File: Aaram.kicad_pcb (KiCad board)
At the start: 2 copper layers, 100 x 100 mm, 52 parts, among them J1 Conn_01x03, J2 Conn_01x02, J3 AC_OUT, J4 SWITCH_IN, J5 5V_OUT, J6 PSU_AC_IN, J8 SPARE_PINS, K1 10A cube relay, K2 10A cube relay, K3 10A cube relay, Q1 BT136-600, Q2 2N2222A, Q3 2N2222A, Q4 2N2222A, U1 ESP32-DevKitC, U2 TLP281-4GB_F_

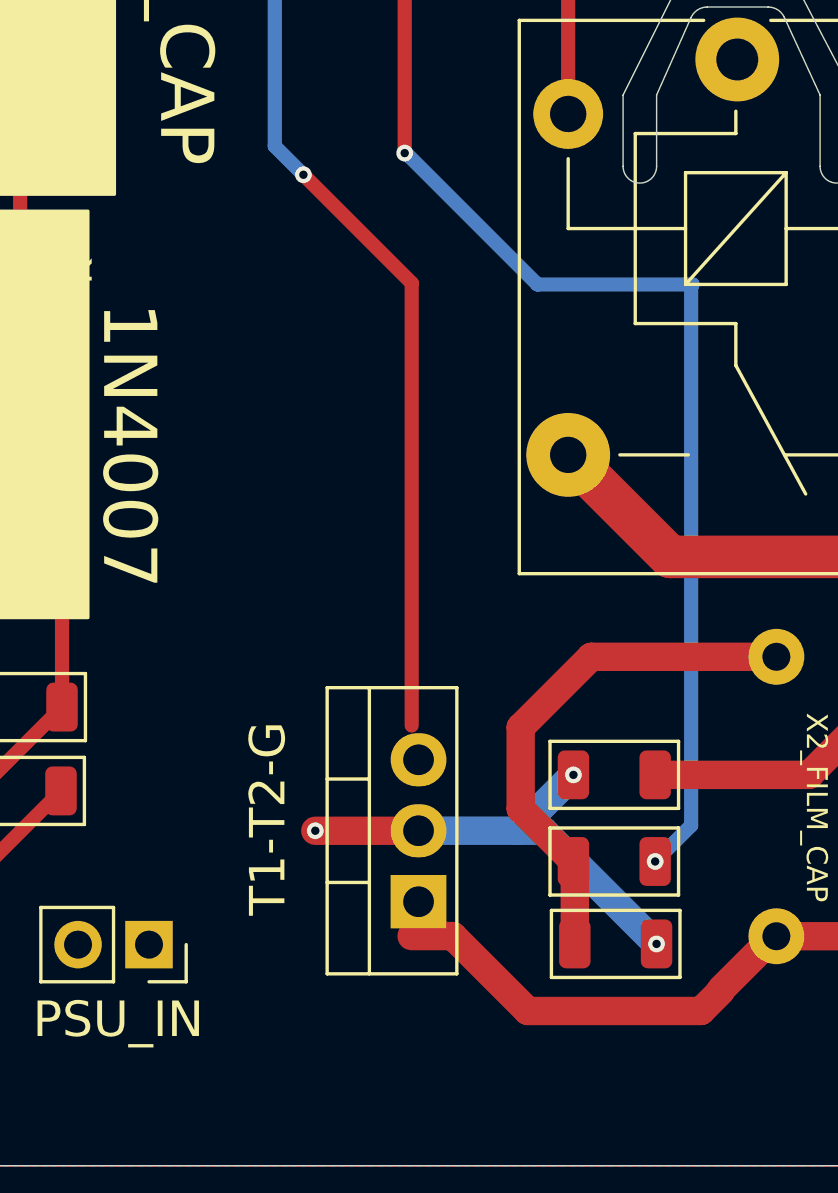
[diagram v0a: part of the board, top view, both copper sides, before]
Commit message: Fixed unconnected tracks of triac
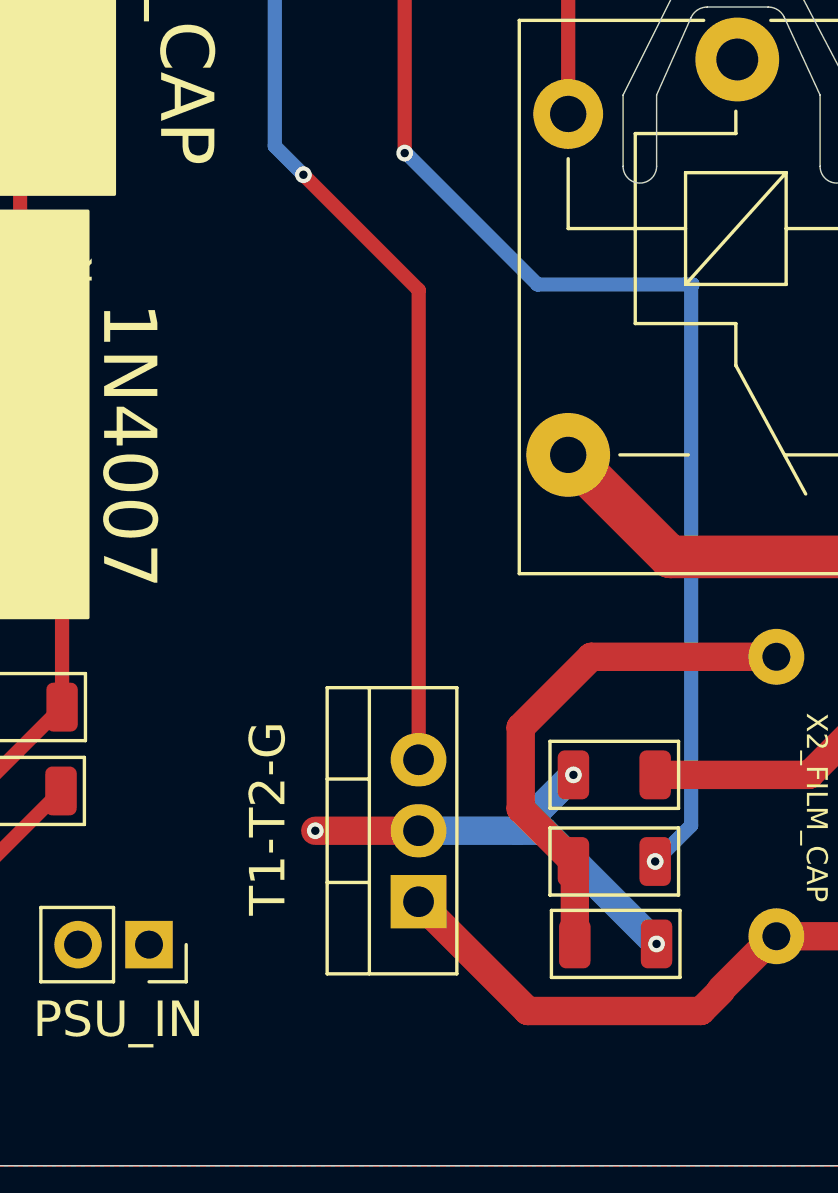
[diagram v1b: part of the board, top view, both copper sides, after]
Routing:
- net Net-(Q1-G): track 58.8 -> 60.1 mm
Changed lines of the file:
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@@
+	)
+	(segment
+		(start 118.313 126.637)
+		(end 117.6 127.35)
+		(width 1.016)
+		(layer "F.Cu")
+		(net 1)
 	)
 	(segment
@@
 	)
 	(segment
-		(start 118.313 126.637)
-		(end 117.6 127.35)
-		(width 1.016)
-		(layer "F.Cu")
-		(net 1)
-	)
-	(segment
-		(start 108.725 124.67)
-		(end 107.245 124.67)
-		(width 1.016)
-		(layer "F.Cu")
-		(net 1)
-	)
-	(segment
-		(start 111.405 127.35)
-		(end 108.725 124.67)
-		(width 1.016)
-		(layer "F.Cu")
-		(net 1)
-	)
-	(segment
 		(start 118.313 126.587)
 		(end 118.313 126.637)
@@
 		(start 117.6 127.35)
 		(end 111.405 127.35)
+		(width 1.016)
+		(layer "F.Cu")
+		(net 1)
+	)
+	(segment
+		(start 111.405 127.35)
+		(end 107.495 123.44)
 		(width 1.016)
 		(layer "F.Cu")
@@
 	)
 	(segment
-		(start 107.25 101.3)
-		(end 107.25 117.135)
+		(start 107.5 101.55)
+		(end 107.5 118.355)
 		(width 0.508)
 		(layer "F.Cu")
@@
 	(segment
 		(start 103.375 97.425)
-		(end 107.25 101.3)
-		(width 0.508)
-		(layer "F.Cu")
+		(end 107.5 101.55)
+		(width 0.508)
+		(layer "F.Cu")
+		(net 40)
+	)
+	(segment
+		(start 107.5 118.355)
+		(end 107.495 118.36)
+		(width 0.508)
+		(layer "F.Cu")

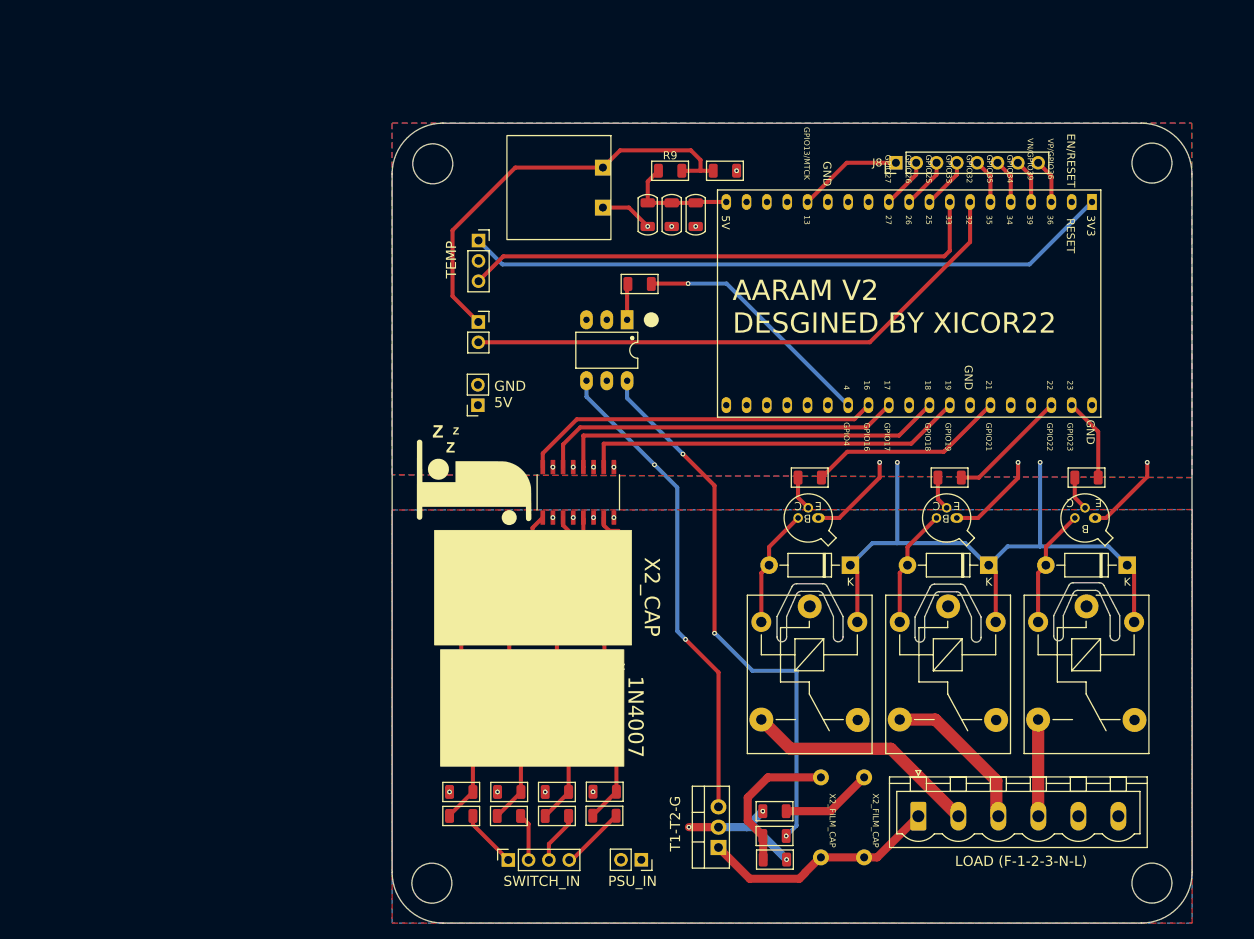
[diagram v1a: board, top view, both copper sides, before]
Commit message: Updated Silkscreen and connections
Moved the fan control from GPIO4 to GPIO 13, made changes to the silkscreen and redid some of the tracks for better layout.
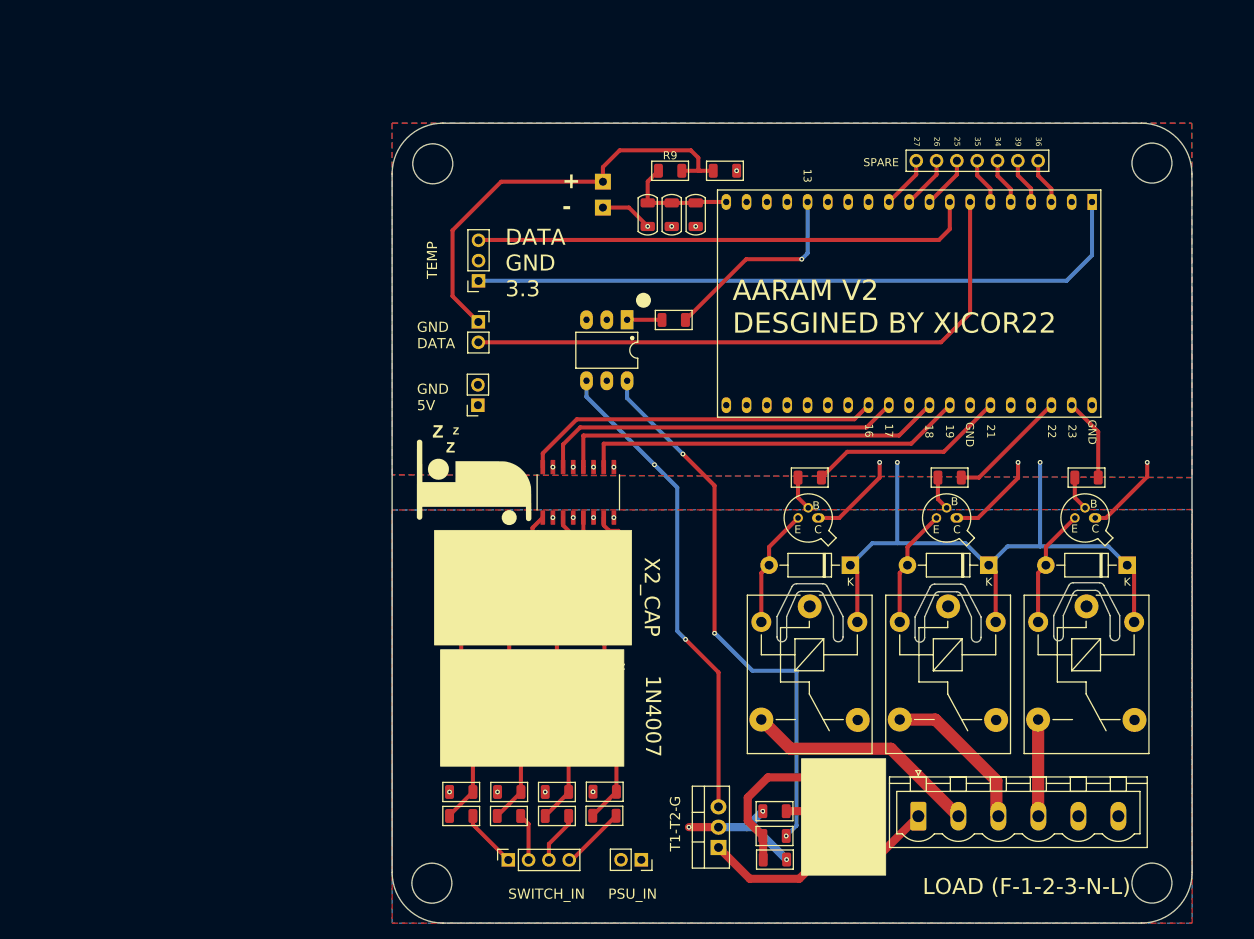
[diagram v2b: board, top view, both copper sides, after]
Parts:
- moved R4 6.20 mm to (101.9, 57.5)
- moved J1 5.05 mm to (77.5, 52.6), turned to 180 degrees
- moved J8 0.25 mm to (129.7, 37.6)
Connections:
- U1 pad 15: SP1 -> T1_Pin
- U1 pad 26: T1_Pin -> unconnected-(U1-ADC2_CH0/GPIO4-Pad26)
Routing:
- net SP1: track 13.1 -> 0.00 mm
- net T1_Pin: track 30.9 -> 25.1 mm
- net S2_Pin: track 71.7 -> 76.9 mm
- net S1_Pin: track 66.6 -> 62.8 mm
- net +3.3V: track 81.2 -> 84.6 mm
- net Net-(J2-Pin_1): track 53.7 -> 54.7 mm
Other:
- board text added: "+ -"
- board text added: "DATA GND 3.3"
- board text added: "GND DATA"
- board text added: "SPARE"

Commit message: Component update
Changed most of the components to use SMD form factor, updated clearance between components in the AC zone and updated the tracks.
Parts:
- C10, C8, C9: footprint PCM_Capacitor_SMD_AKL:C_1206_3216Metric -> PCM_Capacitor_SMD_Handsoldering_AKL:C_1206_3216Metric_Pad1.42x1.75mm
- D1, D2, D3, D4, D5, D6, D7: footprint Diode_THT:D_DO-41_SOD81_P10.16mm_Horizontal -> Diode_SMD:D_SMA_Handsoldering
- Q2, Q3, Q4: footprint PCM_Package_TO_SOT_THT_AKL:TO-18-3_EBC -> PCM_Package_TO_SOT_SMD_AKL:SOT-23_BigPads
- R1, R10, R11, R12, R13, R14, R15, R16, R17, R2, R3, R4, R5, R6, R7, R8, R9: footprint PCM_Resistor_SMD_AKL:R_1206_3216Metric -> PCM_Capacitor_SMD_Handsoldering_AKL:C_1206_3216Metric_Pad1.42x1.75mm
- moved R7 6.07 mm to (112.0, 119.4), turned to 0 degrees
- moved Q1 5.78 mm to (105.2, 118.2)
- moved D3 4.85 mm to (119.5, 86.4)
- moved D1 4.77 mm to (154.1, 86.5)
- moved D2 4.75 mm to (136.8, 86.5)
- moved R5 4.07 mm to (112.1, 115.6)
- moved D4 3.89 mm to (75.4, 104.8)
- moved D5 3.89 mm to (81.4, 104.8)
- moved D6 3.89 mm to (93.3, 104.8)
- moved D7 3.89 mm to (87.4, 104.8)
- moved R6 2.83 mm to (112.1, 123.5), turned to 180 degrees
- moved R11 2.64 mm to (75.3, 113.9)
- moved R13 2.64 mm to (81.3, 113.9)
- moved R15 2.64 mm to (93.3, 113.8)
- moved R17 2.64 mm to (87.3, 113.9)
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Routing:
- net LOAD_F: track 29.9 -> 37.5 mm
- net AC_L: track 16.7 -> 9.27 mm, vias 3 -> 2
- net Net-(C1-Pad1): track 18.7 -> 11.9 mm
- net Net-(Q1-G): track 60.1 -> 53.8 mm, vias 2 -> 1
- net Net-(C4-Pad1): track 11.5 -> 17.2 mm, vias 0 -> 1
- net +5V: track 96.2 -> 101.3 mm, vias 2 -> 5
- net Net-(D6-A): track 10.2 -> 14.0 mm
- net Net-(D4-A): track 10.2 -> 14.0 mm
- net Net-(D5-A): track 10.2 -> 14.0 mm
- net Net-(D7-A): track 10.2 -> 13.9 mm
- net Net-(OC1-Pad6): track 69.5 -> 72.4 mm, vias 3 -> 4
- net GND: track 41.0 -> 39.0 mm
- net Net-(D4-K): track 22.9 -> 24.7 mm
- net Net-(D5-K): track 22.8 -> 24.4 mm
- net D3: track 10.4 -> 8.97 mm
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
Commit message: Updated mostly everything
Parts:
- removed C10, C8, C9: 22uf, PCM_Capacitor_SMD_Handsoldering_AKL:C_1206_3216Metric_Pad1.42x1.75mm
- removed C3, C5: CP_Axial_L10.0mm_D4.5mm_P15.00mm, Xicor_Custom stuff:Axial_Capacitor_P10mm_W4.5mm
- removed D4, D5, D6, D7: 1N4007, Diode_SMD:D_SMA_Handsoldering
- removed G***: LOGO, LOGO
- removed R11, R13: 10K, PCM_Capacitor_SMD_Handsoldering_AKL:C_1206_3216Metric_Pad1.42x1.75mm
- removed R16: 1M, PCM_Capacitor_SMD_Handsoldering_AKL:C_1206_3216Metric_Pad1.42x1.75mm
- added C11: 10uf, PCM_Capacitor_SMD_Handsoldering_AKL:C_1206_3216Metric_Pad1.42x1.75mm, F.Cu at (65.6, 57.4)
- added C12: 10uf, PCM_Capacitor_SMD_Handsoldering_AKL:C_1206_3216Metric_Pad1.42x1.75mm, F.Cu at (65.6, 60.6)
- added C16: 1uf, PCM_Capacitor_SMD_Handsoldering_AKL:C_1206_3216Metric_Pad1.42x1.75mm, F.Cu at (113.7, 47.9)
- added C18: 0.1uf, PCM_Capacitor_SMD_Handsoldering_AKL:C_1206_3216Metric_Pad1.42x1.75mm, F.Cu at (87.7, 40.8)
- added C19: 0.1uf, PCM_Capacitor_SMD_Handsoldering_AKL:C_1206_3216Metric_Pad1.42x1.75mm, F.Cu at (96.2, 49.6)
- added D10: MB6S, PCM_Diode_SMD_AKL:Diode_Bridge_MBS, F.Cu at (108.4, 92.4)
- added D11: MB6S, PCM_Diode_SMD_AKL:Diode_Bridge_MBS, F.Cu at (115.1, 92.4)
- added D8: MB6S, PCM_Diode_SMD_AKL:Diode_Bridge_MBS, F.Cu at (94.8, 92.4)
- added D9: MB6S, PCM_Diode_SMD_AKL:Diode_Bridge_MBS, F.Cu at (101.6, 92.4)
- added F1: Fuse, Xicor_Custom stuff:BLX-A, F.Cu at (43.5, 113.3)
- added J10: Conn_01x03_Socket, Connector_JST:JST_SH_BM03B-SRSS-TB_1x03-1MP_P1.00mm_Vertical, F.Cu at (115.8, 61.1)
- added J11: Conn_01x03_Socket, Connector_JST:JST_SH_BM03B-SRSS-TB_1x03-1MP_P1.00mm_Vertical, F.Cu at (105.1, 61.1)
- added J12: Conn_01x03_Socket, Connector_JST:JST_SH_BM03B-SRSS-TB_1x03-1MP_P1.00mm_Vertical, F.Cu at (105.1, 53.5)
- added J13: Conn_01x03_Socket, Connector_JST:JST_SH_BM03B-SRSS-TB_1x03-1MP_P1.00mm_Vertical, F.Cu at (115.8, 53.5)
- added J7: Conn_01x05, Connector_PinHeader_2.54mm:PinHeader_1x05_P2.54mm_Vertical, F.Cu at (72.6, 22.7)
- added J9: Conn_01x02, Connector_PinSocket_2.54mm:PinSocket_1x02_P2.54mm_Vertical, F.Cu at (22.8, 33.8)
- added R19: 100K, PCM_Resistor_SMD_AKL:R_1206_3216Metric_Pad1.42x1.75mm_HandSolder, F.Cu at (115.7, 82.4)
- added R20: 10K, PCM_Resistor_SMD_AKL:R_1206_3216Metric_Pad1.42x1.75mm_HandSolder, B.Cu at (115.8, 53.6)
- added R21: 10k, PCM_Resistor_SMD_AKL:R_1206_3216Metric_Pad1.42x1.75mm_HandSolder, F.Cu at (96.2, 46.6)
- added R22: 10k, PCM_Resistor_SMD_AKL:R_1206_3216Metric_Pad1.42x1.75mm_HandSolder, F.Cu at (102.9, 40.3)
- added R23: 100K, PCM_Resistor_SMD_AKL:R_1206_3216Metric_Pad1.42x1.75mm_HandSolder, F.Cu at (107.1, 82.4)
- added R25: 10K, PCM_Resistor_SMD_AKL:R_1206_3216Metric_Pad1.42x1.75mm_HandSolder, B.Cu at (105.1, 53.5)
- added R26: 10K, PCM_Resistor_SMD_AKL:R_1206_3216Metric_Pad1.42x1.75mm_HandSolder, B.Cu at (105.1, 61.1)
- added R27: 10K, PCM_Resistor_SMD_AKL:R_1206_3216Metric_Pad1.42x1.75mm_HandSolder, B.Cu at (115.8, 61.1)
- added RV1: Varistor, Xicor_Custom stuff:Varistor_10D431K, F.Cu at (37.5, 93.0)
- added RV2: Varistor, Xicor_Custom stuff:Varistor_10D431K, F.Cu at (69.7, 97.3)
- added RV3: Varistor, Xicor_Custom stuff:Varistor_10D431K, F.Cu at (65.4, 103.9)
- added RV4: Varistor, Xicor_Custom stuff:Varistor_10D431K, F.Cu at (37.5, 84.2)
- added SW1: SW_Push, Xicor_Custom stuff:Tactile switch 6x3, F.Cu at (93.2, 40.8)
- added SW2: SW_Push, Xicor_Custom stuff:SMD Tactile switch, F.Cu at (37.1, 56.1)
- added SW4: SW_Push, Xicor_Custom stuff:Tactile switch 6x3, F.Cu at (99.3, 41.5)
- added U3: ~, Xicor_Custom stuff:Mini_Boost, F.Cu at (34.9, 58.8)
- added U4: ~, Xicor_Custom stuff:TP4056-18650, F.Cu at (51.3, 41.3)
- added U5: TLP281-4GB_F_, Xicor_Custom stuff:SOP127P780X200-16N, F.Cu at (111.4, 72.3)
- C2: footprint Xicor_Custom stuff:Film_Cap_13x13mm_P5.00mm -> PCM_Capacitor_SMD_Handsoldering_AKL:C_1206_3216Metric_Pad1.42x1.75mm
- C6, C7: value CP_Axial_L10.0mm_D4.5mm_P15.00mm -> 10uf; footprint Xicor_Custom stuff:Axial_Capacitor_P10mm_W4.5mm -> PCM_Capacitor_SMD_Handsoldering_AKL:C_1206_3216Metric_Pad1.42x1.75mm
- D1, D2, D3: moved to B.Cu
- J5: value 5V_OUT -> PSU_5V_OUT
- J8: value SPARE_PINS -> USB_C_Receptacle_USB2.0_16P; footprint Connector_PinHeader_2.54mm:PinHeader_1x08_P2.54mm_Vertical -> Connector_USB:USB_C_Receptacle_GCT_USB4105-xx-A_16P_TopMnt_Horizontal
- Q2, Q3, Q4: footprint PCM_Package_TO_SOT_SMD_AKL:SOT-23_BigPads -> PCM_Package_TO_SOT_THT_AKL:TO-18-3_EBC
- R1, R2, R3, R4, R5, R6, R7, R8, R9: footprint PCM_Capacitor_SMD_Handsoldering_AKL:C_1206_3216Metric_Pad1.42x1.75mm -> PCM_Resistor_SMD_AKL:R_1206_3216Metric_Pad1.42x1.75mm_HandSolder
- R10: value 1M -> 10k; footprint PCM_Capacitor_SMD_Handsoldering_AKL:C_1206_3216Metric_Pad1.42x1.75mm -> PCM_Resistor_SMD_AKL:R_1206_3216Metric_Pad1.42x1.75mm_HandSolder
- R12, R14: value 1M -> 5.1k; footprint PCM_Capacitor_SMD_Handsoldering_AKL:C_1206_3216Metric_Pad1.42x1.75mm -> PCM_Resistor_SMD_AKL:R_1206_3216Metric_Pad1.42x1.75mm_HandSolder
- R15, R17: value 10K -> 100K; footprint PCM_Capacitor_SMD_Handsoldering_AKL:C_1206_3216Metric_Pad1.42x1.75mm -> PCM_Resistor_SMD_AKL:R_1206_3216Metric_Pad1.42x1.75mm_HandSolder
- U1: value ESP32-DevKitC -> ESP32-C6-MINI-1/U; footprint Xicor_Custom stuff:ESP32_38Pin -> PCM_Espressif:ESP32-C6-MINI-1
- U2: value TLP281-4GB_F_ -> AZ1117D-3.3TRE1; footprint Xicor_Custom stuff:SOIC127P700X210-16N -> PCM_Package_TO_SOT_SMD_AKL:TO-252-2
- moved J3 111.8 mm to (29.4, 76.3), turned to -90 degrees
- moved K1 93.8 mm to (59.9, 99.1), turned to 180 degrees
- moved D1 90.5 mm to (64.0, 95.6), turned to -90 degrees
- moved R10 82.6 mm to (87.8, 37.8)
- moved R12 81.8 mm to (107.6, 42.0)
- moved R14 81.8 mm to (107.6, 39.0)
- moved C1 81.4 mm to (42.9, 86.7), turned to 90 degrees
- moved J6 77.0 mm to (22.8, 107.7), turned to 90 degrees
- moved R7 72.3 mm to (49.6, 82.8)
- moved R6 69.0 mm to (56.4, 82.8), turned to 0 degrees
- moved C4 68.6 mm to (63.1, 86.7), turned to 90 degrees
- moved Q1 67.5 mm to (50.5, 78.6), turned to 0 degrees
- moved D2 66.1 mm to (72.3, 72.0)
- moved R1 63.7 mm to (90.6, 65.8), turned to 180 degrees
- moved R5 63.3 mm to (55.7, 86.8), turned to 0 degrees
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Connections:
- C6 pad 1: Net-(D6-K) -> GND
- C6 pad 2: AC_N -> +5V
- C7 pad 1: Net-(D7-K) -> GND
- C7 pad 2: AC_N -> +5V
- J1 pad 3: S1_Pin -> Sensor 1
- J2 pad 2: S2_Pin -> Sensor 2
- J3 pad 2: LOAD_1 -> LOAD_2
- J3 pad 3: LOAD_2 -> LOAD_1
- J3 pad 6: AC_L -> Net-(J3-Pin_6)
- J4 pad 1: S1 -> AC_IN_1
- J4 pad 2: S2 -> AC_IN_2
- J4 pad 3: S3 -> AC_IN_3
- J4 pad 4: S4 -> AC_IN_4
- J5 pad 1: +5V -> PSU_5V
- Q2 pad 3: Net-(D1-A) -> Net-(D2-A)
- Q3 pad 3: Net-(D2-A) -> Net-(D3-A)
- Q4 pad 3: Net-(D3-A) -> Net-(D1-A)
- R1 pad 2: D3 -> D2
- R10 pad 1: Net-(D4-A) -> +3.3V
- R10 pad 2: S1 -> Net-(U1-EN/CHIP_PU)
- R12 pad 1: Net-(D5-A) -> GND
- R12 pad 2: S2 -> Net-(J8-CC1)
- R14 pad 1: Net-(D6-A) -> GND
- R14 pad 2: S4 -> Net-(J8-CC2)
- R15 pad 1: AC_N -> Net-(U5-A2)
- R15 pad 2: Net-(D6-A) -> Net-(D9-+)
- R17 pad 1: AC_N -> Net-(U5-A3)
- R2 pad 2: D2 -> D1
- R3 pad 2: D1 -> D3
- U1 pad 1: +3.3V -> GND
- U1 pad 10: SP3 -> SP5
- U1 pad 11: SP2 -> GND
- U1 pad 13: unconnected-(U1-MTDI/GPIO12/ADC2_CH5-Pad13) -> SP1
- U1 pad 15: T1_Pin -> Sensor 1
- U1 pad 16: unconnected-(U1-SD_DATA2/GPIO9-Pad16) -> Sensor 2
- U1 pad 17: unconnected-(U1-SD_DATA3/GPIO10-Pad17) -> USB-
- U1 pad 18: unconnected-(U1-CMD-Pad18) -> USB+
- U1 pad 19: +5V -> AC_IN_1
- U1 pad 2: unconnected-(U1-CHIP_PU-Pad2) -> GND
- U1 pad 20: unconnected-(U1-SD_CLK/GPIO6-Pad20) -> AC_IN_2
- U1 pad 22: unconnected-(U1-SD_DATA1/GPIO8-Pad22) -> Net-(U1-GPIO8)
- U1 pad 23: unconnected-(U1-MTDO/GPIO15/ADC2_CH3-Pad23) -> Net-(U1-GPIO9)
- U1 pad 24: unconnected-(U1-ADC2_CH2/GPIO2-Pad24) -> AC_IN_3
- U1 pad 25: unconnected-(U1-GPIO0/BOOT/ADC2_CH1-Pad25) -> AC_IN_4
- U1 pad 26: unconnected-(U1-ADC2_CH0/GPIO4-Pad26) -> D3
- U1 pad 27: O1 -> D2
- U1 pad 28: O2 -> D1
- U1 pad 29: unconnected-(U1-GPIO5-Pad29) -> T1_Pin
- U1 pad 3: SP8 -> +3.3V
- U1 pad 30: O3 -> unconnected-(U1-U0RXD/GPIO17-Pad30)
- U1 pad 31: O4 -> unconnected-(U1-U0TXD/GPIO16-Pad31)
- U1 pad 32: GND -> unconnected-(U1-NC-Pad32)
- U1 pad 33: D1 -> unconnected-(U1-NC-Pad33)
- U1 pad 36: D2 -> GND
- U1 pad 37: D3 -> GND
- U1 pad 4: SP7 -> unconnected-(U1-NC-Pad4)
- U1 pad 5: SP6 -> SP2
- U1 pad 6: SP5 -> SP3
- U1 pad 7: S2_Pin -> unconnected-(U1-NC-Pad7)
- U1 pad 8: S1_Pin -> Net-(U1-EN/CHIP_PU)
- U2 pad 1: Net-(D4-K) -> GND
- U2 pad 2: AC_N -> +3.3V
- U2 pad 3: Net-(D5-K) -> +5V
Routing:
- net +5V: track 101.3 -> 0.00 mm, vias 5 -> 0
- net +3.3V: track 84.6 -> 0.00 mm
- net S2_Pin: track 76.9 -> 0.00 mm
- net Net-(OC1-Pad6): track 72.4 -> 0.00 mm, vias 4 -> 0
- net S1_Pin: track 62.8 -> 0.00 mm
- net Net-(J2-Pin_1): track 54.7 -> 0.00 mm
- net Net-(Q1-G): track 53.8 -> 0.00 mm, vias 1 -> 0
- net O3: track 48.8 -> 0.00 mm
- net O4: track 48.2 -> 0.00 mm
- net O2: track 45.6 -> 0.00 mm
- net O1: track 44.9 -> 0.00 mm
- net GND: track 39.0 -> 0.00 mm, vias 11 -> 0
- net LOAD_F: track 37.5 -> 0.00 mm
- net LOAD_1: track 29.6 -> 0.00 mm
- net T1_Pin: track 25.1 -> 0.00 mm, vias 1 -> 0
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- added copper zone on B.Cu, net +5V
- added copper zone on F.Cu, net GND
- removed copper zone on F.Cu, net +5V
- removed copper zone on B.Cu, net GND
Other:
- outline, holes or cut-outs redrawn
- board text removed: "+ -"
- board text removed: "1N4007"
- board text removed: "AARAM V2 DESGINED BY XICOR22"
- board text removed: "CURRENT"
- board text removed: "DATA GND 3.3"
- board text removed: "GND 5V"
- board text removed: "GND DATA"
- board text removed: "LOAD (F-1-2-3-N-L)"
- board text removed: "PSU_IN"
- board text removed: "SPARE"
- board text removed: "SWITCH_IN"
- board text removed: "T1-T2-G"
- board text removed: "TEMP"
- board text removed: "X2_CAP"
